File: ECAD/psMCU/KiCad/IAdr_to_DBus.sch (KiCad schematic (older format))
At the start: 16 parts, among them U74 SN74LVC1G126DCK, U75 SN74LVC1G126DCK, U76 SN74LVC1G04DCK, U77 SN74LVC1G04DCK, U78 SN74HC245PW, U79 SN74HC245PW

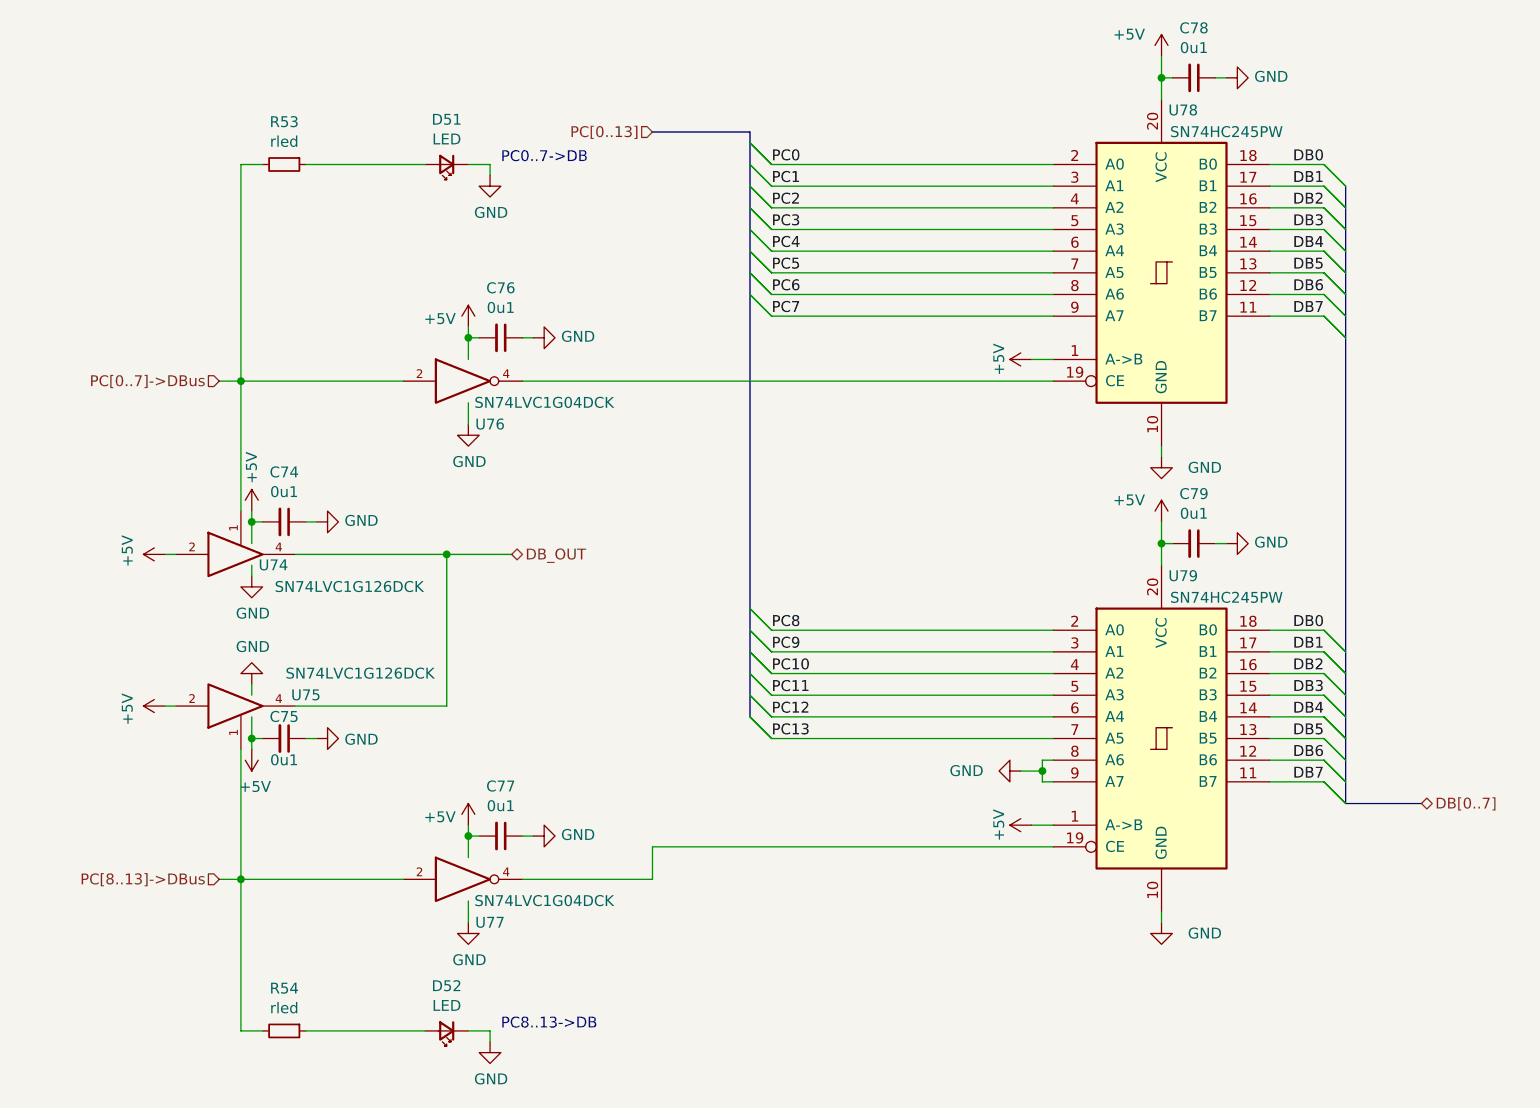
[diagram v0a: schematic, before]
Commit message: Sch: Implemented new Statemachine
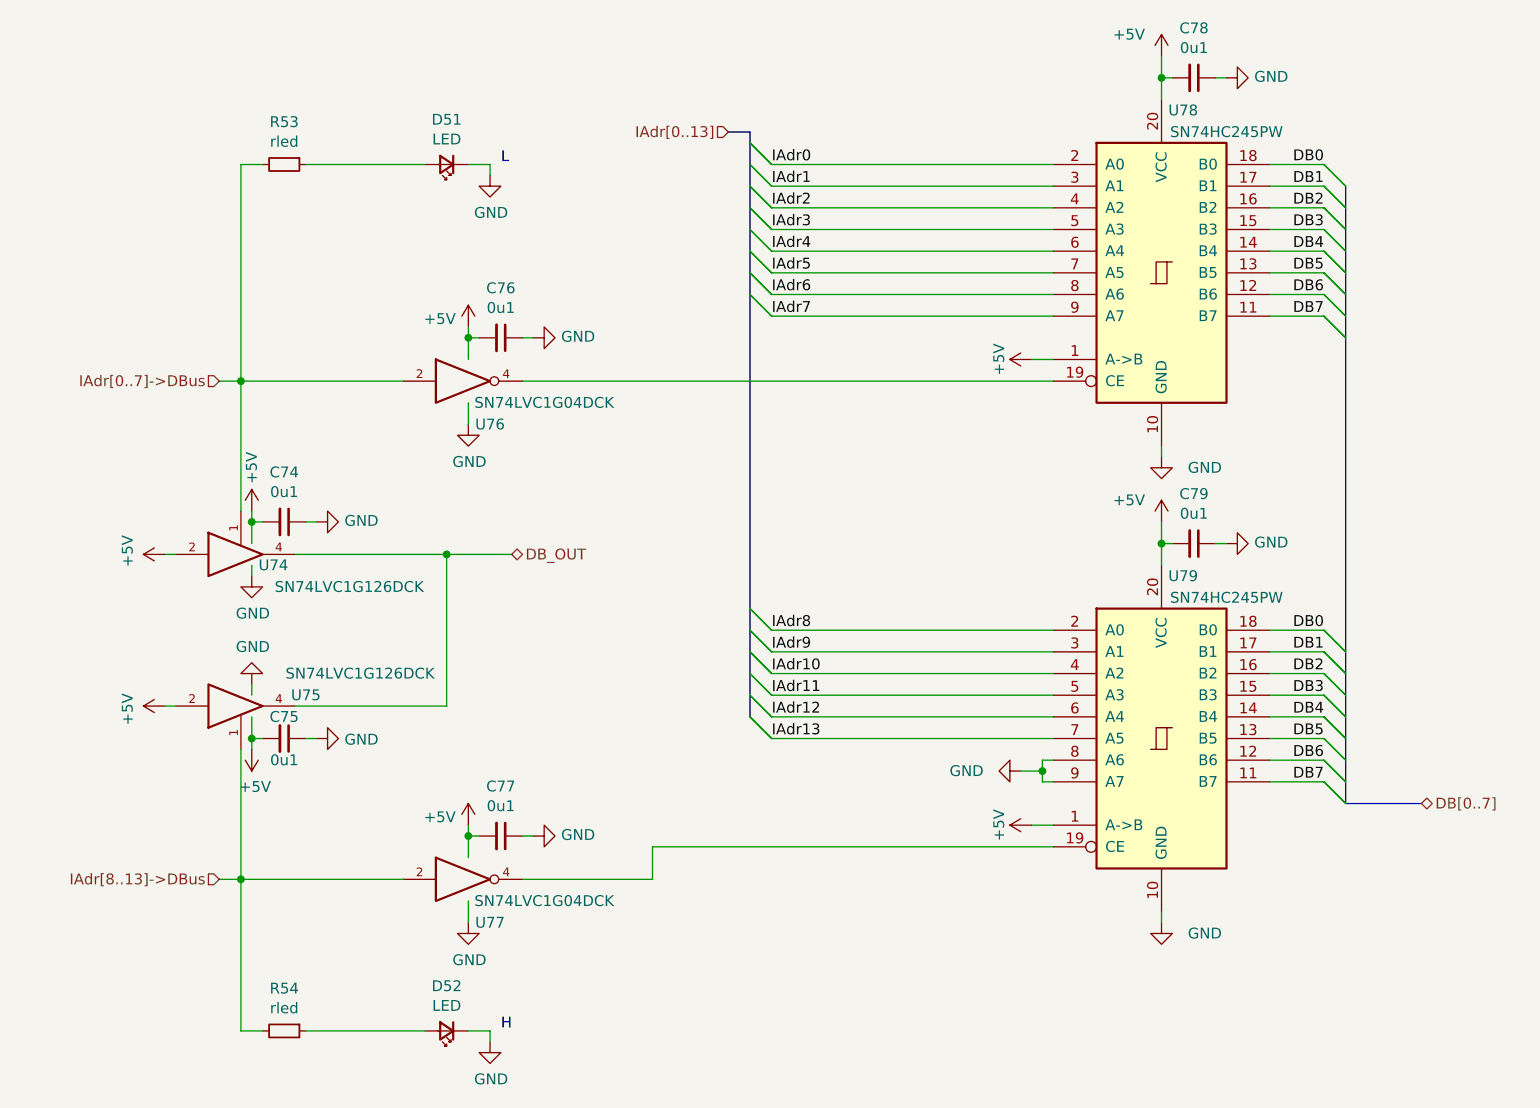
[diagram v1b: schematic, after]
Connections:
- net PC0 renamed IAdr0
- net PC1 renamed IAdr1
- net PC10 renamed IAdr10
- net PC11 renamed IAdr11
- net PC12 renamed IAdr12
- net PC13 renamed IAdr13
- net PC2 renamed IAdr2
- net PC3 renamed IAdr3
- net PC4 renamed IAdr4
- net PC5 renamed IAdr5
- net PC6 renamed IAdr6
- net PC7 renamed IAdr7
- net PC8 renamed IAdr8
- net PC9 renamed IAdr9
- net PC[0..7]->DBus renamed IAdr[0..7]->DBus
- net PC[8..13]->DBus renamed IAdr[8..13]->DBus
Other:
- note added: "H"
- note added: "L"
- note removed: "PC0..7->DB"
- note removed: "PC8..13->DB"
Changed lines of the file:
@@
 $Descr A4 11693 8268
 encoding utf-8
-Sheet 94 97
+Sheet 102 102
 Title "psMCU"
 Date "2022-02-13"
@@
 	4850 2450 4950 2550
 Wire Bus Line
-	4850 1700 4400 1700
+	4850 1700 4750 1700
 Wire Wire Line
 	2550 3750 2550 3700
@@
 	4850 3900 4950 4000
 Text HLabel 2400 2850 0    50   Input ~ 0
-PC[0..7]->DBus
-Text HLabel 4400 1700 0    50   Input ~ 0
-PC[0..13]
+IAdr[0..7]->DBus
+Text HLabel 4750 1700 0    50   Input ~ 0
+IAdr[0..13]
 $Comp
 L power:GND #PWR?
@@
 	2500 5150 2500 4550
 Text HLabel 2400 5150 0    50   Input ~ 0
-PC[8..13]->DBus
+IAdr[8..13]->DBus
 $Comp
 L power:+5V #PWR?
@@
 Wire Wire Line
 	3450 3650 3750 3650
-Wire Wire Line
-	4950 1850 6250 1850
-Wire Wire Line
-	4950 1950 6250 1950
-Wire Wire Line
-	4950 2050 6250 2050
-Wire Wire Line
-	4950 2150 6250 2150
-Wire Wire Line
-	4950 2250 6250 2250
-Wire Wire Line
-	4950 2350 6250 2350
-Wire Wire Line
-	4950 2450 6250 2450
-Wire Wire Line
-	4950 2550 6250 2550
-Wire Wire Line
-	4950 4000 6250 4000
-Wire Wire Line
-	4950 4100 6250 4100
-Wire Wire Line
-	4950 4200 6250 4200
-Wire Wire Line
-	4950 4300 6250 4300
-Wire Wire Line
-	4950 4400 6250 4400
-Wire Wire Line
-	4950 4500 6250 4500
-Text Label 4950 1850 0    50   ~ 0
-PC0
-Text Label 4950 1950 0    50   ~ 0
-PC1
-Text Label 4950 2050 0    50   ~ 0
-PC2
-Text Label 4950 2150 0    50   ~ 0
-PC3
-Text Label 4950 2250 0    50   ~ 0
-PC4
-Text Label 4950 2350 0    50   ~ 0
-PC5
-Text Label 4950 2450 0    50   ~ 0
-PC6
-Text Label 4950 2550 0    50   ~ 0
-PC7
-Text Label 4950 4000 0    50   ~ 0
-PC8
-Text Label 4950 4100 0    50   ~ 0
-PC9
-Text Label 4950 4200 0    50   ~ 0
-PC10
-Text Label 4950 4300 0    50   ~ 0
-PC11
-Text Label 4950 4400 0    50   ~ 0
-PC12
-Text Label 4950 4500 0    50   ~ 0
-PC13
 Wire Wire Line
 	3800 2850 6250 2850
@@
 	2500 5850 2600 5850
 Text Notes 3700 1850 0    50   ~ 0
-PC0..7->DB
+L
 Text Notes 3700 5850 0    50   ~ 0
-PC8..13->DB
+H
+Text Label 4950 1850 0    50   ~ 0
+IAdr0
+Text Label 4950 1950 0    50   ~ 0
+IAdr1
+Text Label 4950 2050 0    50   ~ 0
+IAdr2
+Text Label 4950 2150 0    50   ~ 0
+IAdr3
+Text Label 4950 2250 0    50   ~ 0
+IAdr4
+Text Label 4950 2350 0    50   ~ 0
+IAdr5
+Text Label 4950 2450 0    50   ~ 0
+IAdr6
+Text Label 4950 2550 0    50   ~ 0
+IAdr7
+Text Label 4950 4000 0    50   ~ 0
+IAdr8
+Text Label 4950 4100 0    50   ~ 0
+IAdr9
+Text Label 4950 4200 0    50   ~ 0
+IAdr10
+Text Label 4950 4300 0    50   ~ 0
+IAdr11
+Text Label 4950 4400 0    50   ~ 0
+IAdr12
+Text Label 4950 4500 0    50   ~ 0
+IAdr13
+Wire Wire Line
+	4950 4000 6250 4000
+Wire Wire Line
+	4950 4100 6250 4100
+Wire Wire Line
+	4950 4200 6250 4200
+Wire Wire Line
+	4950 4300 6250 4300
+Wire Wire Line
+	4950 4400 6250 4400
+Wire Wire Line
+	4950 4500 6250 4500
+Wire Wire Line
+	4950 1850 6250 1850
+Wire Wire Line
+	4950 1950 6250 1950
+Wire Wire Line
+	4950 2050 6250 2050
+Wire Wire Line
+	4950 2150 6250 2150
+Wire Wire Line
+	4950 2250 6250 2250
+Wire Wire Line
+	4950 2350 6250 2350
+Wire Wire Line
+	4950 2450 6250 2450
+Wire Wire Line
+	4950 2550 6250 2550
 Wire Bus Line
 	4850 1700 4850 4400
